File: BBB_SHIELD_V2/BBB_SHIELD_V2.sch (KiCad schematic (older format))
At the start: 1 part, among them J1 Screw_Terminal_01x04

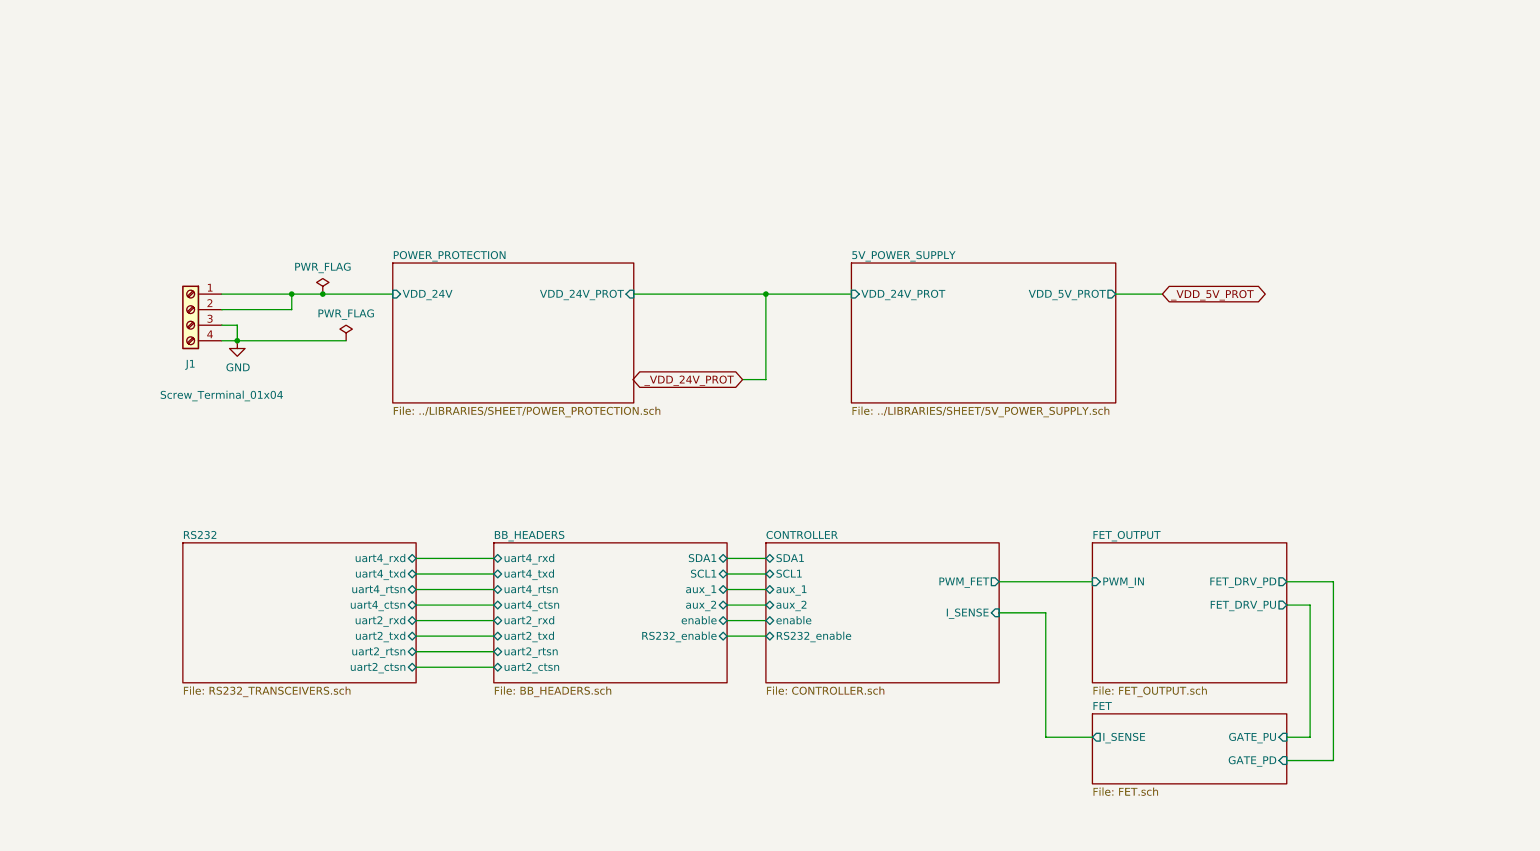
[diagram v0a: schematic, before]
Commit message: Changed to high-side switching of power supply to boards.  Changed footprints to SOIC.  Misc other changes.
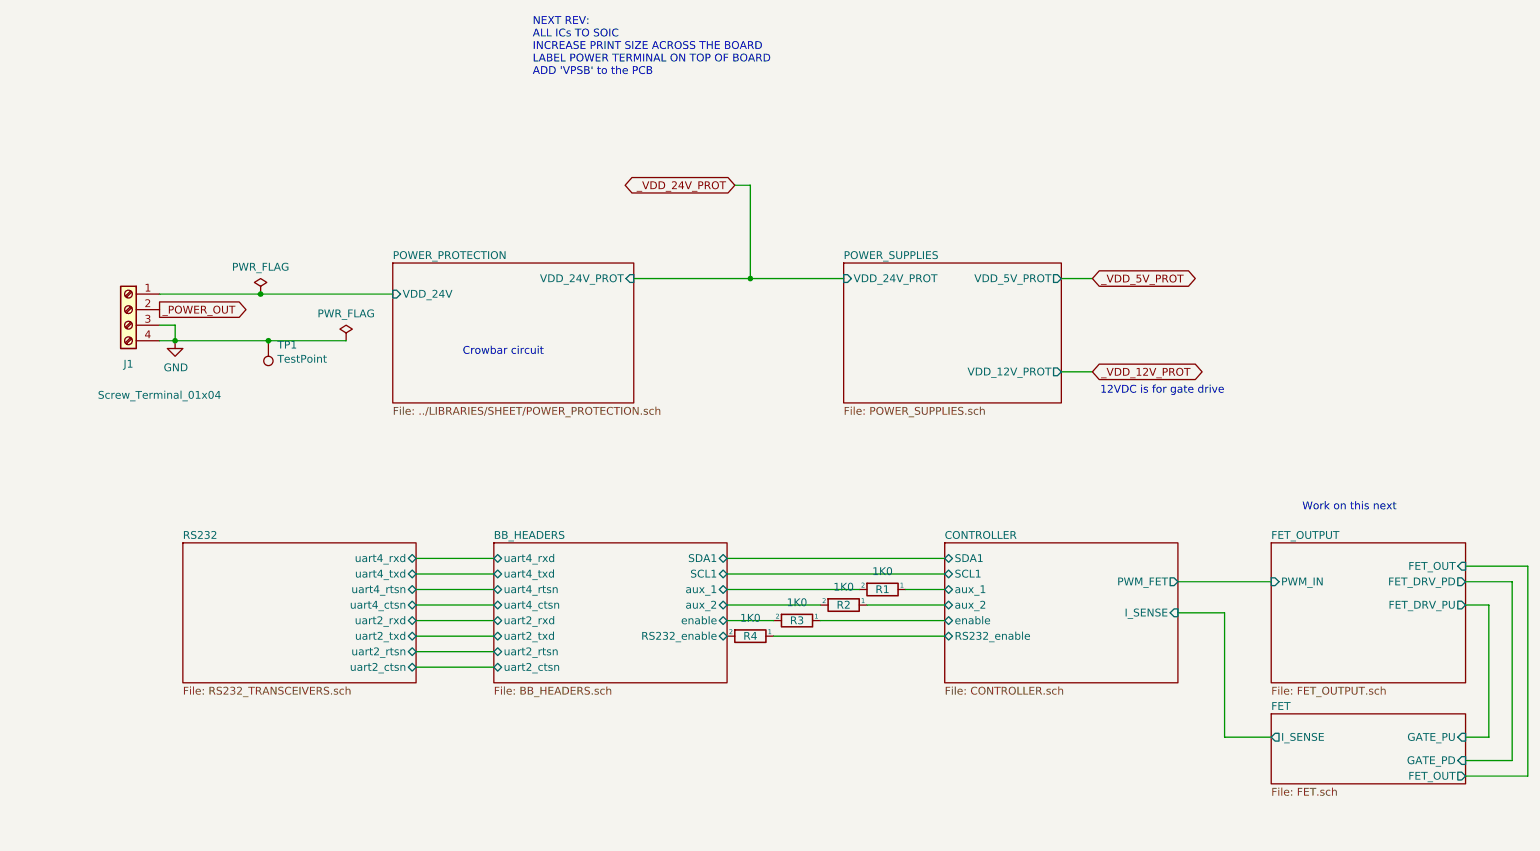
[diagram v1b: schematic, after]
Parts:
- added R1, R2, R3, R4: 1K0, Resistor_SMD:R_0805_2012Metric, symbol CUSTOM_COMPONENTS:R_C
- added TP1: TestPoint, TestPoint:TestPoint_THTPad_D1.0mm_Drill0.5mm, symbol Connector:TestPoint
- J1: NOTES (none) -> BULK, VER 2018-11-25
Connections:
- net BB_HEADERS/RS232_enable: now also R4.2
- net BB_HEADERS/aux_1: now also R1.2
- net BB_HEADERS/aux_2: now also R2.2
- net BB_HEADERS/enable: now also R3.2
- net GND: now also TP1.1
- net POWER_PROTECTION/VDD_24V: no longer J1.2 (Pin_2)
- new net CONTROLLER/RS232_enable: R4.1
- new net CONTROLLER/aux_1: R1.1
- new net CONTROLLER/aux_2: R2.1
- new net CONTROLLER/enable: R3.1
- new net _POWER_OUT: J1.2 (Pin_2)
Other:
- note added: "12VDC is for gate drive"
- note added: "Crowbar circuit"
- note added: "NEXT REV: \nALL ICs TO SOIC\nINCREASE PRINT SIZE ACROSS THE BOARD\nLABEL POWER TERMINAL ON TOP OF BOARD\nADD 'VPSB' to the PCB"
- note added: "Work on this next"
- moved on the sheet: J1
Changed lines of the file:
@@
 $Descr A4 11693 8268
 encoding utf-8
-Sheet 1 11
+Sheet 1 12
 Title ""
 Date ""
@@
 $EndDescr
 $Sheet
-S 6300 2200 1700 900
-U 5B952F96
-F0 "5V_POWER_SUPPLY" 50
-F1 "../LIBRARIES/SHEET/5V_POWER_SUPPLY.sch" 50
-F2 "VDD_5V_PROT" O R 8000 2400 50
-F3 "VDD_24V_PROT" I L 6300 2400 50
-$EndSheet
-$Sheet
 S 3350 2200 1550 900
 U 5B953ACE
@@
 F1 "../LIBRARIES/SHEET/POWER_PROTECTION.sch" 50
 F2 "VDD_24V" I L 3350 2400 50
-F3 "VDD_24V_PROT" I R 4900 2400 50
+F3 "VDD_24V_PROT" I R 4900 2300 50
 $EndSheet
 $Comp
 L Connector:Screw_Terminal_01x04 J1
 U 1 1 5B95BE4E
-P 2050 2500
-F 0 "J1" H 2050 2150 50  0000 C CNN
-F 1 "Screw_Terminal_01x04" H 1850 1950 50  0000 C CNN
-F 2 "CUSTOM_FOOTPRINTS:OSTTA044163" H 2050 2500 50  0001 C CNN
-F 3 "~" H 2050 2500 50  0001 C CNN
-	1    2050 2500
+P 1650 2500
+F 0 "J1" H 1650 2150 50  0000 C CNN
+F 1 "Screw_Terminal_01x04" H 1450 1950 50  0000 C CNN
+F 2 "CUSTOM_FOOTPRINTS:OSTTA044163" H 1650 2500 50  0001 C CNN
+F 3 "" H 1650 2500 50  0001 C CNN
+F 4 "BULK, VER 2018-11-25" H -400 0   50  0001 C CNN "NOTES"
+	1    1650 2500
 	-1   0    0    -1
 $EndComp
 Wire Wire Line
-	2250 2600 2350 2600
-Wire Wire Line
-	2350 2600 2350 2700
-Wire Wire Line
-	2350 2700 2250 2700
+	1850 2600 1950 2600
+Wire Wire Line
+	1950 2600 1950 2700
+Wire Wire Line
+	1950 2700 1850 2700
 $Comp
 L power:PWR_FLAG #FLG01
 U 1 1 5B95D9AF
-P 2900 2400
-F 0 "#FLG01" H 2900 2475 50  0001 C CNN
-F 1 "PWR_FLAG" H 2900 2574 50  0000 C CNN
-F 2 "" H 2900 2400 50  0001 C CNN
-F 3 "~" H 2900 2400 50  0001 C CNN
-	1    2900 2400
+P 2500 2400
+F 0 "#FLG01" H 2500 2475 50  0001 C CNN
+F 1 "PWR_FLAG" H 2500 2574 50  0000 C CNN
+F 2 "" H 2500 2400 50  0001 C CNN
+F 3 "~" H 2500 2400 50  0001 C CNN
+	1    2500 2400
 	1    0    0    -1
 $EndComp
-Wire Wire Line
-	2900 2400 3350 2400
 $Comp
 L power:GND #PWR01
 U 1 1 5B95F37B
-P 2350 2700
-F 0 "#PWR01" H 2350 2450 50  0001 C CNN
-F 1 "GND" H 2355 2527 50  0000 C CNN
-F 2 "" H 2350 2700 50  0001 C CNN
-F 3 "" H 2350 2700 50  0001 C CNN
-	1    2350 2700
+P 1950 2700
+F 0 "#PWR01" H 1950 2450 50  0001 C CNN
+F 1 "GND" H 1955 2527 50  0000 C CNN
+F 2 "" H 1950 2700 50  0001 C CNN
+F 3 "" H 1950 2700 50  0001 C CNN
+	1    1950 2700
 	1    0    0    -1
 $EndComp
-Connection ~ 2350 2700
-Wire Wire Line
-	4900 2400 5750 2400
-Wire Wire Line
-	8000 2400 8300 2400
-Text GLabel 8300 2400 2    50   BiDi ~ 0
+Connection ~ 1950 2700
+Text GLabel 7850 2300 2    50   BiDi ~ 0
 _VDD_5V_PROT
-Text GLabel 5600 2950 0    50   BiDi ~ 0
+Text GLabel 5550 1700 0    50   BiDi ~ 0
 _VDD_24V_PROT
-Wire Wire Line
-	5600 2950 5750 2950
-Wire Wire Line
-	5750 2950 5750 2400
-Connection ~ 5750 2400
-Wire Wire Line
-	5750 2400 6300 2400
-$Sheet
-S 7850 4000 1250 900
+$Sheet
+S 9000 4000 1250 900
 U 5B9E7514
 F0 "FET_OUTPUT" 50
 F1 "FET_OUTPUT.sch" 50
-F2 "PWM_IN" I L 7850 4250 50
-F3 "FET_DRV_PU" O R 9100 4400 50
-F4 "FET_DRV_PD" O R 9100 4250 50
-$EndSheet
-$Sheet
-S 5750 4000 1500 900
+F2 "PWM_IN" I L 9000 4250 50
+F3 "FET_DRV_PU" O R 10250 4400 50
+F4 "FET_DRV_PD" O R 10250 4250 50
+F5 "FET_OUT" I R 10250 4150 50
+$EndSheet
+$Sheet
+S 6900 4000 1500 900
 U 5B9EA430
 F0 "CONTROLLER" 50
 F1 "CONTROLLER.sch" 50
-F2 "PWM_FET" O R 7250 4250 50
-F3 "I_SENSE" I R 7250 4450 50
-F4 "SDA1" B L 5750 4100 50
-F5 "SCL1" B L 5750 4200 50
-F6 "aux_1" B L 5750 4300 50
-F7 "aux_2" B L 5750 4400 50
-F8 "enable" B L 5750 4500 50
-F9 "RS232_enable" B L 5750 4600 50
+F2 "PWM_FET" O R 8400 4250 50
+F3 "I_SENSE" I R 8400 4450 50
+F4 "SDA1" B L 6900 4100 50
+F5 "SCL1" B L 6900 4200 50
+F6 "aux_1" B L 6900 4300 50
+F7 "aux_2" B L 6900 4400 50
+F8 "enable" B L 6900 4500 50
+F9 "RS232_enable" B L 6900 4600 50
 $EndSheet
 $Sheet
@@
 $EndSheet
 Wire Wire Line
-	7250 4250 7850 4250
-$Sheet
-S 7850 5100 1250 450
+	8400 4250 9000 4250
+$Sheet
+S 9000 5100 1250 450
 U 5BA13116
 F0 "FET" 50
 F1 "FET.sch" 50
-F2 "GATE_PU" I R 9100 5250 50
-F3 "GATE_PD" I R 9100 5400 50
-F4 "I_SENSE" O L 7850 5250 50
-$EndSheet
-Wire Wire Line
-	9100 4250 9400 4250
-Wire Wire Line
-	9400 5400 9100 5400
-Wire Wire Line
-	9400 4250 9400 5400
-Wire Wire Line
-	9100 5250 9250 5250
-Wire Wire Line
-	9250 5250 9250 4400
-Wire Wire Line
-	9250 4400 9100 4400
-Wire Wire Line
-	7250 4450 7550 4450
-Wire Wire Line
-	7550 4450 7550 5250
-Wire Wire Line
-	7550 5250 7850 5250
-Connection ~ 2900 2400
-Wire Wire Line
-	2250 2400 2700 2400
-Wire Wire Line
-	2700 2400 2700 2500
-Connection ~ 2700 2400
-Wire Wire Line
-	2700 2400 2900 2400
-Wire Wire Line
-	2250 2500 2700 2500
-Wire Wire Line
-	5500 4100 5750 4100
+F2 "GATE_PU" I R 10250 5250 50
+F3 "GATE_PD" I R 10250 5400 50
+F4 "I_SENSE" O L 9000 5250 50
+F5 "FET_OUT" O R 10250 5500 50
+$EndSheet
+Wire Wire Line
+	10250 4250 10550 4250
+Wire Wire Line
+	10550 5400 10250 5400
+Wire Wire Line
+	10550 4250 10550 5400
+Wire Wire Line
+	10250 5250 10400 5250
+Wire Wire Line
+	10400 5250 10400 4400
+Wire Wire Line
+	10400 4400 10250 4400
+Wire Wire Line
+	8400 4450 8700 4450
+Wire Wire Line
+	8700 4450 8700 5250
+Wire Wire Line
+	8700 5250 9000 5250
+Connection ~ 2500 2400
 $Sheet
 S 2000 4000 1500 900
@@
 	4000 4800 3500 4800
 Wire Wire Line
-	5500 4200 5750 4200
-Wire Wire Line
-	5750 4300 5500 4300
-Wire Wire Line
-	5500 4400 5750 4400
-Wire Wire Line
-	5750 4500 5500 4500
-Wire Wire Line
-	5500 4600 5750 4600
+	6900 4300 6650 4300
 $Comp
 L power:PWR_FLAG #FLG02
@@
 	1    0    0    -1
 $EndComp
-Wire Wire Line
-	3050 2700 2350 2700
+Text Notes 4250 1000 0    50   ~ 0
+NEXT REV: \nALL ICs TO SOIC\nINCREASE PRINT SIZE ACROSS THE BOARD\nLABEL POWER TERMINAL ON TOP OF BOARD\nADD 'VPSB' to the PCB
+Wire Wire Line
+	5500 4100 6900 4100
+Wire Wire Line
+	5500 4200 6900 4200
+$Comp
+L CUSTOM_COMPONENTS:R_C R1
+U 1 1 5C14F7E5
+P 6500 4300
+F 0 "R1" V 6500 4300 50  0000 C CNN
+F 1 "1K0" V 6384 4300 50  0000 C CNN
+F 2 "Resistor_SMD:R_0805_2012Metric" V 6430 4300 50  0001 C CNN
+F 3 "" H 6500 4300 50  0001 C CNN
+	1    6500 4300
+	0    1    1    0
+$EndComp
+$Comp
+L CUSTOM_COMPONENTS:R_C R2
+U 1 1 5C14F83C
+P 6250 4400
+F 0 "R2" V 6250 4400 50  0000 C CNN
+F 1 "1K0" V 6134 4400 50  0000 C CNN
+F 2 "Resistor_SMD:R_0805_2012Metric" V 6180 4400 50  0001 C CNN
+F 3 "" H 6250 4400 50  0001 C CNN
+	1    6250 4400
+	0    1    1    0
+$EndComp
+$Comp
+L CUSTOM_COMPONENTS:R_C R3
+U 1 1 5C14F8B9
+P 5950 4500
+F 0 "R3" V 5950 4500 50  0000 C CNN
+F 1 "1K0" V 5834 4500 50  0000 C CNN
+F 2 "Resistor_SMD:R_0805_2012Metric" V 5880 4500 50  0001 C CNN
+F 3 "" H 5950 4500 50  0001 C CNN
+	1    5950 4500
+	0    1    1    0
+$EndComp
+$Comp
+L CUSTOM_COMPONENTS:R_C R4
+U 1 1 5C14F936
+P 5650 4600
+F 0 "R4" V 5650 4600 50  0000 C CNN
+F 1 "1K0" V 5534 4600 50  0000 C CNN
+F 2 "Resistor_SMD:R_0805_2012Metric" V 5580 4600 50  0001 C CNN
+F 3 "" H 5650 4600 50  0001 C CNN
+	1    5650 4600
+	0    1    1    0
+$EndComp
+Wire Wire Line
+	6350 4300 5500 4300
+Wire Wire Line
+	6100 4400 5500 4400
+Wire Wire Line
+	5800 4500 5500 4500
+Wire Wire Line
+	5800 4600 6900 4600
+Wire Wire Line
+	6100 4500 6900 4500
+Wire Wire Line
+	6400 4400 6900 4400
+$Sheet
+S 6250 2200 1400 900
+U 5C3BCB20
+F0 "POWER_SUPPLIES" 50
+F1 "POWER_SUPPLIES.sch" 50
+F2 "VDD_24V_PROT" I L 6250 2300 50
+F3 "VDD_5V_PROT" O R 7650 2300 50
+F4 "VDD_12V_PROT" O R 7650 2900 50
+$EndSheet
+Text GLabel 7850 2900 2    50   BiDi ~ 0
+_VDD_12V_PROT
+Wire Wire Line
+	4900 2300 5650 2300
+Wire Wire Line
+	5550 1700 5650 1700
+Wire Wire Line
+	5650 1700 5650 2300
+Connection ~ 5650 2300
+Wire Wire Line
+	5650 2300 6250 2300
+Wire Wire Line
+	7650 2300 7850 2300
+Wire Wire Line
+	7650 2900 7850 2900
+Wire Wire Line
+	2500 2400 3350 2400
+Wire Wire Line
+	1850 2400 2500 2400
+Text GLabel 1850 2500 2    50   Output ~ 0
+_POWER_OUT
+Text Notes 7900 3050 0    50   ~ 0
+12VDC is for gate drive
+Text Notes 3800 2800 0    50   ~ 0
+Crowbar circuit
+Text Notes 9200 3800 0    50   ~ 0
+Work on this next
+Wire Wire Line
+	10650 4150 10650 5500
+Wire Wire Line
+	10650 5500 10250 5500
+Wire Wire Line
+	10250 4150 10650 4150
+Wire Wire Line
+	1950 2700 2550 2700
+$Comp
+L Connector:TestPoint TP1
+U 1 1 5D136AA5
+P 2550 2700
+F 0 "TP1" H 2492 2727 50  0000 R CNN
+F 1 "TestPoint" H 2492 2818 50  0000 R CNN
+F 2 "TestPoint:TestPoint_THTPad_D1.0mm_Drill0.5mm" H 2750 2700 50  0001 C CNN
+F 3 "~" H 2750 2700 50  0001 C CNN
+	1    2550 2700
+	-1   0    0    1
+$EndComp
+Connection ~ 2550 2700
+Wire Wire Line
+	2550 2700 3050 2700
 $EndSCHEMATC

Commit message: Rev 2 problem fixes.
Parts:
- J1: NOTES BULK, VER 2018-11-25 -> VER,2019-07-16,REUSE
- R1, R2, R3, R4: value 1K0 -> 1K; DKPN (none) -> 541-3977-2-ND; MFG (none) -> VISHAY; MFGPN (none) -> CRCW08051K00FKEAC; NOTES (none) -> VER,2019-07-17,REEL
- TP1: footprint TestPoint:TestPoint_THTPad_D1.0mm_Drill0.5mm -> Connector_PinHeader_1.27mm:PinHeader_1x02_P1.27mm_Vertical; symbol Connector:TestPoint -> Connector:TestPoint_2Pole
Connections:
- net GND: now also TP1.2
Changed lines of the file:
@@
 F 2 "CUSTOM_FOOTPRINTS:OSTTA044163" H 1650 2500 50  0001 C CNN
 F 3 "" H 1650 2500 50  0001 C CNN
-F 4 "BULK, VER 2018-11-25" H -400 0   50  0001 C CNN "NOTES"
+F 4 "VER,2019-07-16,REUSE" H -400 0   50  0001 C CNN "NOTES"
 	1    1650 2500
 	-1   0    0    -1
@@
 P 6500 4300
 F 0 "R1" V 6500 4300 50  0000 C CNN
-F 1 "1K0" V 6384 4300 50  0000 C CNN
+F 1 "1K" V 6384 4300 50  0000 C CNN
 F 2 "Resistor_SMD:R_0805_2012Metric" V 6430 4300 50  0001 C CNN
 F 3 "" H 6500 4300 50  0001 C CNN
+F 4 "VER,2019-07-17,REEL" H 0   0   50  0001 C CNN "NOTES"
+F 5 "541-3977-2-ND" H 0   0   50  0001 C CNN "DKPN"
+F 6 "VISHAY" H 0   0   50  0001 C CNN "MFG"
+F 7 "CRCW08051K00FKEAC" H 0   0   50  0001 C CNN "MFGPN"
 	1    6500 4300
 	0    1    1    0
@@
 P 6250 4400
 F 0 "R2" V 6250 4400 50  0000 C CNN
-F 1 "1K0" V 6134 4400 50  0000 C CNN
+F 1 "1K" V 6134 4400 50  0000 C CNN
 F 2 "Resistor_SMD:R_0805_2012Metric" V 6180 4400 50  0001 C CNN
 F 3 "" H 6250 4400 50  0001 C CNN
+F 4 "VER,2019-07-17,REEL" H 0   0   50  0001 C CNN "NOTES"
+F 5 "541-3977-2-ND" H 0   0   50  0001 C CNN "DKPN"
+F 6 "VISHAY" H 0   0   50  0001 C CNN "MFG"
+F 7 "CRCW08051K00FKEAC" H 0   0   50  0001 C CNN "MFGPN"
 	1    6250 4400
 	0    1    1    0
@@
 P 5950 4500
 F 0 "R3" V 5950 4500 50  0000 C CNN
-F 1 "1K0" V 5834 4500 50  0000 C CNN
+F 1 "1K" V 5834 4500 50  0000 C CNN
 F 2 "Resistor_SMD:R_0805_2012Metric" V 5880 4500 50  0001 C CNN
 F 3 "" H 5950 4500 50  0001 C CNN
+F 4 "VER,2019-07-17,REEL" H 0   0   50  0001 C CNN "NOTES"
+F 5 "541-3977-2-ND" H 0   0   50  0001 C CNN "DKPN"
+F 6 "VISHAY" H 0   0   50  0001 C CNN "MFG"
+F 7 "CRCW08051K00FKEAC" H 0   0   50  0001 C CNN "MFGPN"
 	1    5950 4500
 	0    1    1    0
@@
 P 5650 4600
 F 0 "R4" V 5650 4600 50  0000 C CNN
-F 1 "1K0" V 5534 4600 50  0000 C CNN
+F 1 "1K" V 5534 4600 50  0000 C CNN
 F 2 "Resistor_SMD:R_0805_2012Metric" V 5580 4600 50  0001 C CNN
 F 3 "" H 5650 4600 50  0001 C CNN
+F 4 "VER,2019-07-17,REEL" H 0   0   50  0001 C CNN "NOTES"
+F 5 "541-3977-2-ND" H 0   0   50  0001 C CNN "DKPN"
+F 6 "VISHAY" H 0   0   50  0001 C CNN "MFG"
+F 7 "CRCW08051K00FKEAC" H 0   0   50  0001 C CNN "MFGPN"
 	1    5650 4600
 	0    1    1    0
@@
 Wire Wire Line
 	10250 4150 10650 4150
+$Comp
+L Connector:TestPoint_2Pole TP1
+U 1 1 5D136AA5
+P 2550 2900
+F 0 "TP1" H 2492 2927 50  0000 R CNN
+F 1 "TestPoint" H 2492 3018 50  0000 R CNN
+F 2 "Connector_PinHeader_1.27mm:PinHeader_1x02_P1.27mm_Vertical" H 2750 2900 50  0001 C CNN
+F 3 "~" H 2750 2900 50  0001 C CNN
+	1    2550 2900
+	0    -1   -1   0
+$EndComp
 Wire Wire Line
 	1950 2700 2550 2700
-$Comp
-L Connector:TestPoint TP1
-U 1 1 5D136AA5
-P 2550 2700
-F 0 "TP1" H 2492 2727 50  0000 R CNN
-F 1 "TestPoint" H 2492 2818 50  0000 R CNN
-F 2 "TestPoint:TestPoint_THTPad_D1.0mm_Drill0.5mm" H 2750 2700 50  0001 C CNN
-F 3 "~" H 2750 2700 50  0001 C CNN
-	1    2550 2700
-	-1   0    0    1
-$EndComp
 Connection ~ 2550 2700
 Wire Wire Line
 	2550 2700 3050 2700
+$Comp
+L power:GND #PWR0104
+U 1 1 5D4C2DA8
+P 2550 3100
+F 0 "#PWR0104" H 2550 2850 50  0001 C CNN
+F 1 "GND" H 2555 2927 50  0000 C CNN
+F 2 "" H 2550 3100 50  0001 C CNN
+F 3 "" H 2550 3100 50  0001 C CNN
+	1    2550 3100
+	1    0    0    -1
+$EndComp
 $EndSCHEMATC
